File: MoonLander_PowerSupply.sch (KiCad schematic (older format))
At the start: 11 parts, among them IC1 MCP73831/2, IC2 BU33SD5

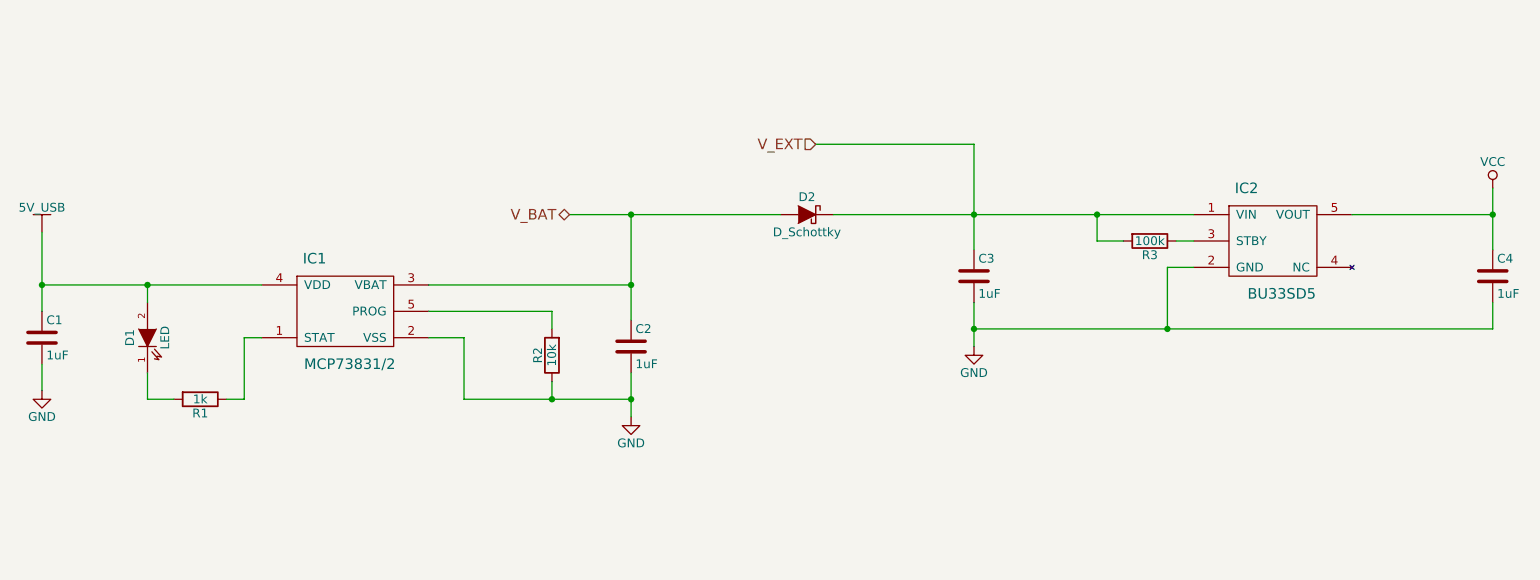
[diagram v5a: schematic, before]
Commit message: bypass battery if USB connected
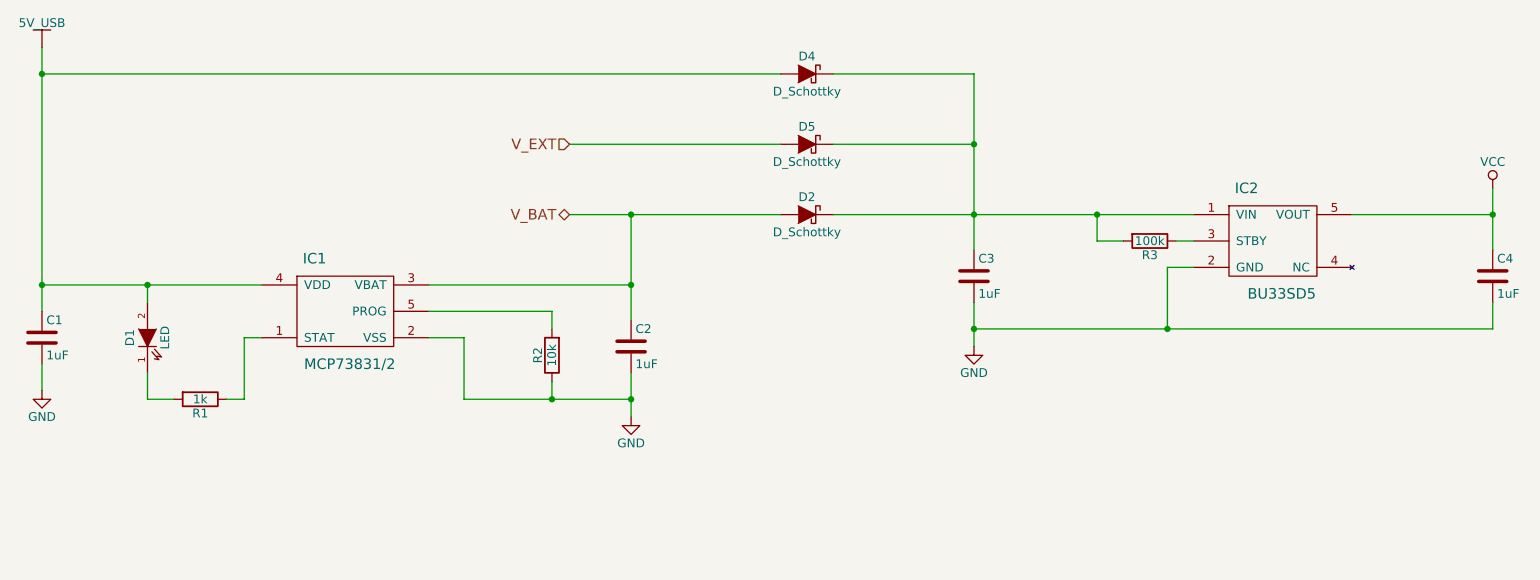
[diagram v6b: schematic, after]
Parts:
- added D4, D5: D_Schottky, Diodes_SMD:SOD-323, symbol D_Schottky
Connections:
- net 5V_USB: now also D4.2 (A)
- net V_EXT: now also D5.2 (A); no longer C3.1, D2.1 (K), IC2.1 (VIN), R3.2
- new net: C3.1, D2.1 (K), D4.1 (K), D5.1 (K), IC2.1 (VIN), R3.2
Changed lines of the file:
@@
 $EndComp
 Wire Wire Line
-	1750 3000 1750 3450
-$Comp
-L GND #PWR06
+	1750 1950 1750 2100
+Wire Wire Line
+	1750 2100 1750 3300
+Wire Wire Line
+	1750 3300 1750 3450
+$Comp
+L GND #PWR7
 U 1 1 565F7639
 P 1750 3900
-F 0 "#PWR06" H 1750 3650 50  0001 C CNN
+F 0 "#PWR7" H 1750 3650 50  0001 C CNN
 F 1 "GND" H 1750 3750 50  0000 C CNN
 F 2 "" H 1750 3900 50  0000 C CNN
@@
 	1750 3750 1750 3900
 $Comp
-L 5V_USB #PWR07
+L 5V_USB #PWR6
 U 1 1 565F7A7B
-P 1750 3000
-F 0 "#PWR07" H 1750 2850 50  0001 C CNN
-F 1 "5V_USB" H 1750 3140 50  0000 C CNN
-F 2 "" H 1750 3000 60  0000 C CNN
-F 3 "" H 1750 3000 60  0000 C CNN
-	1    1750 3000
+P 1750 1950
+F 0 "#PWR6" H 1750 1800 50  0001 C CNN
+F 1 "5V_USB" H 1750 2090 50  0000 C CNN
+F 2 "" H 1750 1950 60  0000 C CNN
+F 3 "" H 1750 1950 60  0000 C CNN
+	1    1750 1950
 	1    0    0    -1
 $EndComp
@@
 $EndComp
 $Comp
-L GND #PWR08
+L GND #PWR9
 U 1 1 56603249
 P 7050 3650
-F 0 "#PWR08" H 7050 3400 50  0001 C CNN
+F 0 "#PWR9" H 7050 3400 50  0001 C CNN
 F 1 "GND" H 7050 3500 50  0000 C CNN
 F 2 "" H 7050 3650 50  0000 C CNN
@@
 $EndComp
 Wire Wire Line
-	7050 3400 7050 3650
-Wire Wire Line
-	7050 2500 7050 3100
+	7050 3400 7050 3550
+Wire Wire Line
+	7050 3550 7050 3650
+Wire Wire Line
+	7050 2100 7050 2500
+Wire Wire Line
+	7050 2500 7050 2900
+Wire Wire Line
+	7050 2900 7050 3100
 Connection ~ 7050 2900
 Wire Wire Line
-	5100 2900 5100 3500
-Text HLabel 6150 2500 0    60   Input ~ 0
+	5100 2900 5100 3300
+Wire Wire Line
+	5100 3300 5100 3500
+Text HLabel 4750 2500 0    60   Input ~ 0
 V_EXT
 $Comp
@@
 	7900 3050 7750 3050
 Wire Wire Line
-	7750 3050 7750 2900
+	7750 2900 7750 3050
 Connection ~ 7750 2900
 Wire Wire Line
@@
 	8150 3200 8150 3550
 Wire Wire Line
-	7050 3550 10000 3550
+	7050 3550 8150 3550
+Wire Wire Line
+	8150 3550 10000 3550
 Connection ~ 7050 3550
 Wire Wire Line
 	9200 2900 10000 2900
 Wire Wire Line
-	10000 2750 10000 3100
+	10000 2750 10000 2900
+Wire Wire Line
+	10000 2900 10000 3100
 $Comp
 L C C4
@@
 Connection ~ 10000 2900
 $Comp
-L VCC #PWR09
+L VCC #PWR10
 U 1 1 565FD3E2
 P 10000 2750
-F 0 "#PWR09" H 10000 2600 50  0001 C CNN
+F 0 "#PWR10" H 10000 2600 50  0001 C CNN
 F 1 "VCC" H 10000 2900 50  0000 C CNN
 F 2 "" H 10000 2750 50  0000 C CNN
@@
 $EndComp
 Wire Wire Line
-	6150 2500 7050 2500
-Wire Wire Line
-	4750 2900 5950 2900
-Wire Wire Line
-	6250 2900 8300 2900
+	4750 2900 5100 2900
+Wire Wire Line
+	5100 2900 5950 2900
+Wire Wire Line
+	6250 2900 7050 2900
+Wire Wire Line
+	7050 2900 7750 2900
+Wire Wire Line
+	7750 2900 8300 2900
 Connection ~ 1750 3300
 $Comp
@@
 $EndComp
 Wire Wire Line
-	1750 3300 3000 3300
+	1750 3300 2350 3300
+Wire Wire Line
+	2350 3300 3000 3300
 Wire Wire Line
 	2350 3300 2350 3400
@@
 	4650 3850 4650 3950
 Wire Wire Line
-	4150 3950 5100 3950
+	4150 3950 4650 3950
+Wire Wire Line
+	4650 3950 5100 3950
 Wire Wire Line
 	4150 3950 4150 3600
@@
 	4150 3600 3950 3600
 Wire Wire Line
-	5100 3800 5100 4050
+	5100 3800 5100 3950
+Wire Wire Line
+	5100 3950 5100 4050
 Connection ~ 4650 3950
 Connection ~ 5100 3300
 $Comp
-L GND #PWR010
+L GND #PWR8
 U 1 1 56658982
 P 5100 4050
-F 0 "#PWR010" H 5100 3800 50  0001 C CNN
+F 0 "#PWR8" H 5100 3800 50  0001 C CNN
 F 1 "GND" H 5100 3900 50  0000 C CNN
 F 2 "" H 5100 4050 50  0000 C CNN
@@
 $EndComp
 Connection ~ 5100 3950
+$Comp
+L D_Schottky D5
+U 1 1 569166D4
+P 6100 2500
+F 0 "D5" H 6100 2600 50  0000 C CNN
+F 1 "D_Schottky" H 6100 2400 50  0000 C CNN
+F 2 "Diodes_SMD:SOD-323" H 6100 2500 50  0001 C CNN
+F 3 "" H 6100 2500 50  0000 C CNN
+	1    6100 2500
+	-1   0    0    -1
+$EndComp
+Wire Wire Line
+	6250 2500 7050 2500
+Wire Wire Line
+	5950 2500 4750 2500
+$Comp
+L D_Schottky D4
+U 1 1 56916799
+P 6100 2100
+F 0 "D4" H 6100 2200 50  0000 C CNN
+F 1 "D_Schottky" H 6100 2000 50  0000 C CNN
+F 2 "Diodes_SMD:SOD-323" H 6100 2100 50  0001 C CNN
+F 3 "" H 6100 2100 50  0000 C CNN
+	1    6100 2100
+	-1   0    0    -1
+$EndComp
+Wire Wire Line
+	6250 2100 7050 2100
+Connection ~ 7050 2500
+Wire Wire Line
+	1750 2100 5950 2100
+Connection ~ 1750 2100
 $EndSCHEMATC

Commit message: added some silk
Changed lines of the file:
@@
 $EndComp
 Wire Wire Line
-	1750 1950 1750 2100
-Wire Wire Line
-	1750 2100 1750 3300
-Wire Wire Line
-	1750 3300 1750 3450
+	1750 1950 1750 3450
 $Comp
 L GND #PWR7
@@
 $EndComp
 Wire Wire Line
-	7050 3400 7050 3550
-Wire Wire Line
-	7050 3550 7050 3650
-Wire Wire Line
-	7050 2100 7050 2500
-Wire Wire Line
-	7050 2500 7050 2900
-Wire Wire Line
-	7050 2900 7050 3100
+	7050 3400 7050 3650
+Wire Wire Line
+	7050 2100 7050 3100
 Connection ~ 7050 2900
 Wire Wire Line
-	5100 2900 5100 3300
-Wire Wire Line
-	5100 3300 5100 3500
+	5100 2900 5100 3500
 Text HLabel 4750 2500 0    60   Input ~ 0
 V_EXT
@@
 	7900 3050 7750 3050
 Wire Wire Line
-	7750 2900 7750 3050
+	7750 3050 7750 2900
 Connection ~ 7750 2900
 Wire Wire Line
@@
 	8150 3200 8150 3550
 Wire Wire Line
-	7050 3550 8150 3550
-Wire Wire Line
-	8150 3550 10000 3550
+	7050 3550 10000 3550
 Connection ~ 7050 3550
 Wire Wire Line
 	9200 2900 10000 2900
 Wire Wire Line
-	10000 2750 10000 2900
-Wire Wire Line
-	10000 2900 10000 3100
+	10000 2750 10000 3100
 $Comp
 L C C4
@@
 $EndComp
 Wire Wire Line
-	4750 2900 5100 2900
-Wire Wire Line
-	5100 2900 5950 2900
-Wire Wire Line
-	6250 2900 7050 2900
-Wire Wire Line
-	7050 2900 7750 2900
-Wire Wire Line
-	7750 2900 8300 2900
+	4750 2900 5950 2900
+Wire Wire Line
+	6250 2900 8300 2900
 Connection ~ 1750 3300
 $Comp
@@
 $EndComp
 Wire Wire Line
-	1750 3300 2350 3300
-Wire Wire Line
-	2350 3300 3000 3300
+	1750 3300 3000 3300
 Wire Wire Line
 	2350 3300 2350 3400
@@
 	4650 3850 4650 3950
 Wire Wire Line
-	4150 3950 4650 3950
-Wire Wire Line
-	4650 3950 5100 3950
+	4150 3950 5100 3950
 Wire Wire Line
 	4150 3950 4150 3600
@@
 	4150 3600 3950 3600
 Wire Wire Line
-	5100 3800 5100 3950
-Wire Wire Line
-	5100 3950 5100 4050
+	5100 3800 5100 4050
 Connection ~ 4650 3950
 Connection ~ 5100 3300
